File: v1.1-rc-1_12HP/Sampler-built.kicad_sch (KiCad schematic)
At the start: 274 parts, among them J10 Eurorack_Power_10pin_Unshroud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, J11 3.5mm_Mono_Switched, J12 3.5mm_Mono_Switched, J13 3.5mm_Mono_Switched, J14 3.5mm_Mono_Switched, J15 3.5mm_Mono_Switched, J16 3.5mm_Mono_Switched, J17 3.5mm_Mono_Switched, J2 3.5mm_Mono_Switched, J3 Conn_01x04, J4 Conn_02x04, J6 3.5mm_Mono_Switched, J7 3.5mm_Mono_Switched, J8 3.5mm_Mono_Switched, J9 3.5mm_Mono_Switched, U1 TL072H, U10 TL072H, U11 TL072H, U12 TL072H, U13 AP62200WU-7, U15 NJM2068, U16 NJM2068, U17 AZ1117CR-3.3TRG1, U18 STS SD card w/adaptor, U2 STM32F746IE, U3 TL072H, U4 SDRAM_IS42S16400J-6BLI-TR, U5 TL072H, U6 NCP51460SN33, U7 TL072H, U8 TL072H, U9 PCM3060PW, Y1 16MHz_18pF_FA238

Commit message: Proofed and fixed v1.1rc1_12HP schematic. Some schematic TODO left
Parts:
- removed C16, C20, C83, C84: 10nF_0402_16V, 4ms_Capacitor:C_0402, symbol 4ms_Capacitor:10nF_0402_16V
- removed C43: 1uF_0603_25V, 4ms_Capacitor:C_0603, symbol 4ms_Capacitor:1uF_0603_25V
- removed C50: 2.2uF_0603_25V, 4ms_Capacitor:C_0603, symbol 4ms_Capacitor:2.2uF_0603_25V
- removed C65, C66: 100nF_0402_50V, 4ms_Capacitor:C_0402, symbol 4ms_Capacitor:100nF_0402_50V
- removed D10, D11, D12, D13, D14, D2, D27, D28, D30, D4, D5, D6, D8, D9: BAT54S, 4ms_Package_SOT:SOT23-3_PO132, symbol 4ms_Diode:BAT54S
- removed R37: 68Ω_0402, 4ms_Resistor:R_0402, symbol 4ms_Resistor_0402:68Ω_0402
- removed R38: 10k_0603, 4ms_Resistor:R_0603, symbol 4ms_Resistor_0603:10k_0603
- removed R39, R9: 2k_0402, 4ms_Resistor:R_0402, symbol 4ms_Resistor_0402:2k_0402
- removed R69, R72: 1k_0603, 4ms_Resistor:R_0603, symbol 4ms_Resistor_0603:1k_0603
- removed R76: 47k_0603, 4ms_Resistor:R_0603, symbol 4ms_Resistor_0603:47k_0603
- removed S1, S2: SW_Push_PTS526 SM15 SMTR2 LFS, 4ms_Switch:Button_Tact_PTS526, symbol 4ms_Switch:SW_Push_PTS526 SM15 SMTR2 LFS
- removed U17: AZ1117CR-3.3TRG1, 4ms_Package_SOT:SOT89-3, symbol 4ms_Regulator:AZ1117CR-3.3TRG1
- removed unit 2 of U7
- added C? (x2): 100nF_0402_50V, 4ms_Capacitor:C_0402, symbol 4ms_Capacitor:100nF_0402_50V
- C39: value 10nF_0402_16V -> 0.1uF_0603_16V; footprint 4ms_Capacitor:C_0402 -> 4ms_Capacitor:C_0603; symbol 4ms_Capacitor:10nF_0402_16V -> 4ms_Capacitor:0.1uF_0603_16V; Display 10nF -> 0.1uF; JLCPCB ID C15195 -> C14663; Manufacturer Yageo -> AVX Corporation; Part Number CC0402KRX7R7BB103 -> 0603YC104KAT2A; Specifications 10nF, Min. 16V 10%, X7R or X5R or similar -> 0.1uF, Min. 16V 10%, X7R or X5R or similar
- R29: value 10k_0603 -> 20k_0603; symbol 4ms_Resistor_0603:10k_0603 -> 4ms_Resistor_0603:20k_0603; Display 10k -> 20k; JLCPCB ID C98220 -> C105575; Part Number RC0603FR-0710KL -> RC0603FR-0720KL; Specifications 10k, 1%, 1/10W, 0603 -> 20k, 1%, 1/10W, 0603
- R64, R68: value 1k_0603 -> 2k_0402; footprint 4ms_Resistor:R_0603 -> 4ms_Resistor:R_0402; symbol 4ms_Resistor_0603:1k_0603 -> 4ms_Resistor_0402:2k_0402; Display 1k -> 2k; JLCPCB ID C22548 -> C60488; Part Number RC0603FR-071KL -> RC0402FR-072KL; Specifications 1k, 1%, 1/10W, 0603 -> 2k, 1%, 1/16W, 0402
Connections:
- net +12V: now also C?.1
- net -12VA: now also C?.1
- net A0: now also R2.2; no longer R1.1
- net A1: now also R12.2; no longer R11.1
- net A2: now also R19.2; no longer R18.1
- net A6: now also C39.1
- net D12: now also C54.1, R74.2
- net D2: now also C19.1, D7.3 (AK), R58.2
- net DEBUG2: now also J4.5 (Pin_5)
- net DEBUG3: now also J4.7 (Pin_7)
- net GND: now also J13.3 (SW), J14.3 (SW), J4.2 (Pin_2), J4.4 (Pin_4), J4.6 (Pin_6), J4.8 (Pin_8), C?.2, C?.2
- net UART_RX: now also J4.3 (Pin_3)
- net UART_TX: now also J4.1 (Pin_1)
- net BOOT0: now reaches R8.2, U2.D6 (BOOT)
- net NRST: now reaches C15.2, U2.J1 (NRST)
- net at C82.1, D1.3 (AK), R1.2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: no longer R15.2, R2.2, R21.2
- net at R29.2: now also C3.2, R57.1, U15.5 (+)
- net at Bank_But1.8 (B): now also R64.2
- net at R68.2: now also REV_BUT1.7 (R)
- net at REV_BUT1.2 (POLE-A): now also R36.2
- net at C6.1, R56.1, U15.7: now also R18.1; no longer R19.2
- net +5VA renamed +5V
- net USB_DM: no longer names the net of U2.C15 (PA11)
- net USB_DP: no longer names the net of U2.B15 (PA12)
- net USB_ID: no longer names the net of U2.D15 (PA10)
- net USB_VBUS: no longer names the net of U2.E15 (PA9)
- new net: C1.1, POT_PITCH1.2 (Center), R11.1
- new net: R1.1, R15.2, R21.2
- new net: R11.2, U1.5 (+)
- no-connect marks 64 -> 66
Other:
- note added: "4ms Sampler (Built)"
- note added: "Note: do not use the second half of this opamp (U16) for anything."
- note added: "TODO: Consolidate CV op-amps based on where they are placed on PCB. Use a single opamp if needed (most likely for PitchCV)"
- note added: "TODO: Use single op-amps for pots"
- note added: "TODO: make all of these like Pitch Pot"
- note added: "TODO: make all of these like StartCV"
- note removed: "4ms Sampler Kit"
- note removed: "I2C4_SCL"
- note removed: "I2C4_SDA"
- note removed: "SPI2_MISO"
- note removed: "SPI2_MOSI"
- note removed: "SPI2_NSS"
- note removed: "SPI2_SCK"
- moved on the sheet: C1, C12, C13, C14, C15, C17, C18, C19, C21, C22, C23, C24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

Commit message: v1.1-rc1-12HP: part placement and routing ip
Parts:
- removed C47, C87, C88: 10nF_0402_16V, 4ms_Capacitor:C_0402, symbol 4ms_Capacitor:10nF_0402_16V
- removed C? (x2): 100nF_0402_50V, 4ms_Capacitor:C_0402, symbol 4ms_Capacitor:100nF_0402_50V
- removed D18, D31, D32: BAT54S, 4ms_Package_SOT:SOT23-3_PO132, symbol 4ms_Diode:BAT54S
- removed unit 3 of U7
- added C87, C88: 100nF_0402_50V, 4ms_Capacitor:C_0402, symbol 4ms_Capacitor:100nF_0402_50V
- added unit 1 of U14
- added unit 3 of U14
- C35: renamed from C13; value 0.1uF_0603_16V -> 100nF_0402_50V; footprint 4ms_Capacitor:C_0603 -> 4ms_Capacitor:C_0402; symbol 4ms_Capacitor:0.1uF_0603_16V -> 4ms_Capacitor:100nF_0402_50V; Alt JLCPCB ID (none) -> C77020; JLCPCB ID C14663 -> C307331; Manufacturer AVX Corporation -> Murata; Part Number 0603YC104KAT2A -> GRM155R71H104KE14D; Specifications 0.1uF, Min. 16V 10%, X7R or X5R or similar -> 0.1uF, Min. 50V 10%, X7R or X5R or similar
- C37: renamed from C14; value 0.1uF_0603_16V -> 100nF_0402_50V; footprint 4ms_Capacitor:C_0603 -> 4ms_Capacitor:C_0402; symbol 4ms_Capacitor:0.1uF_0603_16V -> 4ms_Capacitor:100nF_0402_50V; Alt JLCPCB ID (none) -> C77020; JLCPCB ID C14663 -> C307331; Manufacturer AVX Corporation -> Murata; Part Number 0603YC104KAT2A -> GRM155R71H104KE14D; Specifications 0.1uF, Min. 16V 10%, X7R or X5R or similar -> 0.1uF, Min. 50V 10%, X7R or X5R or similar
- C38: renamed from C17; value 0.1uF_0603_16V -> 100nF_0402_50V; footprint 4ms_Capacitor:C_0603 -> 4ms_Capacitor:C_0402; symbol 4ms_Capacitor:0.1uF_0603_16V -> 4ms_Capacitor:100nF_0402_50V; Alt JLCPCB ID (none) -> C77020; JLCPCB ID C14663 -> C307331; Manufacturer AVX Corporation -> Murata; Part Number 0603YC104KAT2A -> GRM155R71H104KE14D; Specifications 0.1uF, Min. 16V 10%, X7R or X5R or similar -> 0.1uF, Min. 50V 10%, X7R or X5R or similar
- C40: renamed from C18; value 0.1uF_0603_16V -> 100nF_0402_50V; footprint 4ms_Capacitor:C_0603 -> 4ms_Capacitor:C_0402; symbol 4ms_Capacitor:0.1uF_0603_16V -> 4ms_Capacitor:100nF_0402_50V; Alt JLCPCB ID (none) -> C77020; JLCPCB ID C14663 -> C307331; Manufacturer AVX Corporation -> Murata; Part Number 0603YC104KAT2A -> GRM155R71H104KE14D; Specifications 0.1uF, Min. 16V 10%, X7R or X5R or similar -> 0.1uF, Min. 50V 10%, X7R or X5R or similar
- R13, R3, R35, R5, R64, R68: value 2k_0402 -> 2k_0603; footprint 4ms_Resistor:R_0402 -> 4ms_Resistor:R_0603; symbol 4ms_Resistor_0402:2k_0402 -> 4ms_Resistor_0603:2k_0603; JLCPCB ID C60488 -> C105576; Part Number RC0402FR-072KL -> RC0603FR-072KL; Specifications 2k, 1%, 1/16W, 0402 -> 2k, 1%, 1/10W, 0603
- R36: value 10k_0402 -> 10k_0603; footprint 4ms_Resistor:R_0402 -> 4ms_Resistor:R_0603; symbol 4ms_Resistor_0402:10k_0402 -> 4ms_Resistor_0603:10k_0603; JLCPCB ID C60490 -> C98220; Part Number RC0402FR-0710KL -> RC0603FR-0710KL; Specifications 10k, 1%, 1/16W, 0402 -> 10k, 1%, 1/10W, 0603
- renumbered C21 to C1, C31 to C10, C33 to C11, C35 to C12, C36 to C13, C37 to C14, C38 to C17, C79 to C18, C23 to C2, C4 to C21, C89 to C23, C5 to C24, C10 to C25, C11 to C26, C91 to C27, C92 to C28, C24 to C3, C93 to C30, C95 to C31, C96 to C33, C42 to C36, C25 to C4, C3 to C42, C46 to C43, C6 to C46, C53 to C47, C26 to C5, C94 to C50, C40 to C53, C27 to C6, C7 to C65, C9 to C66, C28 to C7, C2 to C79, C1 to C83, C12 to C84, C30 to C9, R31 to R4, R4 to R9, U10 to U1, U1 to U10, U5 to U10, U3 to U14, U10 to U3, U7 to U5
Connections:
- net +12V: now also C87.1, U14.8 (V+)
- net -12VA: now also C88.1, U14.4 (V-)
- net A3: now also R23.2; no longer R22.1
- net A4: now also R28.2; no longer R27.1
- net A5: now also R81.2; no longer R30.1
- net A7: now also R41.2; no longer R40.1
- net A8: now also R34.2; no longer R33.1
- net A9: now also R46.2; no longer R45.1
- net GND: now also U16.3 (+), C87.2, C88.2, U14.2 (-); no longer U16.5 (+)
- net at R20.2, R26.2: now also R27.1; no longer R28.2
- net at C84.2, R62.2, R63.1: now also U16.7; no longer U16.1
- net at R16.2, R24.2: now also R30.1; no longer R81.2
- net at C84.1, R61.2, R62.1: now also U16.6 (-); no longer U16.2 (-)
- net at R17.2, R25.2: now also R33.1; no longer R34.2
- net at R45.2: now also U3.3 (+); no longer U3.5 (+)
- net at R60.2: now also U16.5 (+); no longer U16.3 (+)
- net at R17.1: now also J9.1 (SIG); no longer J7.1 (SIG)
- net at C79.1, POT_SAMP1.2 (Center): now also R45.1; no longer R46.2
- net at C97.1, D15.3 (AK), R18.2: now also U14.5 (+); no longer U14.3 (+)
- net at C85.1, D26.3 (AK), R33.2: now also U5.5 (+); no longer U5.3 (+)
- net at R20.1: now also J7.1 (SIG); no longer J9.1 (SIG)
- new net: C66.1, POT_LENGTH1.2 (Center), R22.1
- new net: R46.1, U3.1, U3.2 (-)
- new net: U14.1, U14.3 (+)
- new net: C65.1, POT_START1.2 (Center), R40.1
- new net: R34.1, U5.6 (-), U5.7
- new net: R19.1, U14.6 (-), U14.7
- new net: U16.1, U16.2 (-)
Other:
- note removed: "Length_Pot"
- note removed: "Pitch_Pot"
- note removed: "Sample_Pot"
- note removed: "Start_Pot"
- note removed: "TODO: make all of these like Pitch Pot"
- note removed: "TODO: make all of these like StartCV"
- moved on the sheet: C42, C46, C65, C66, C79, C97, D15, J6, J7, J8, J9, POT_LENGTH1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

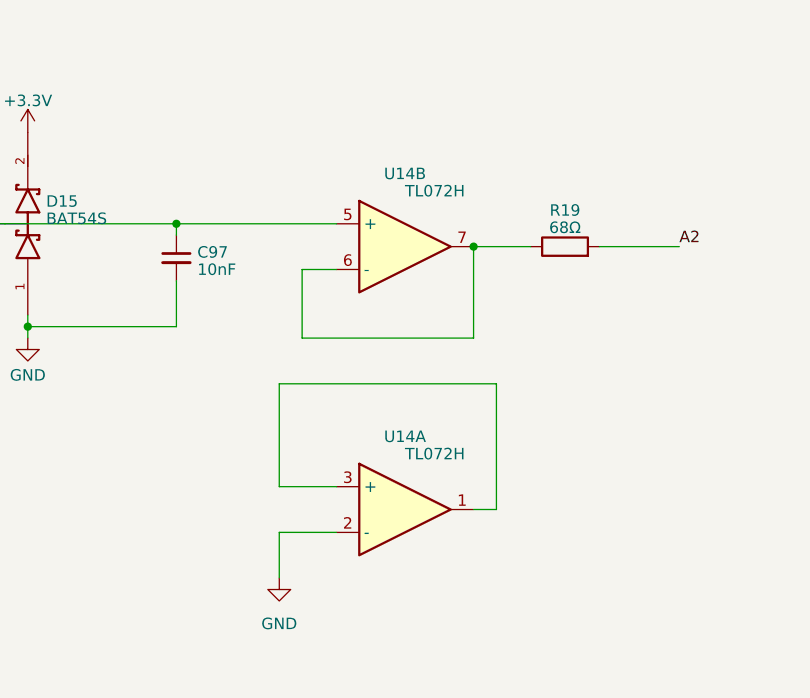
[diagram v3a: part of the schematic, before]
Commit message: Updates to pcb / routing for noise mitigation
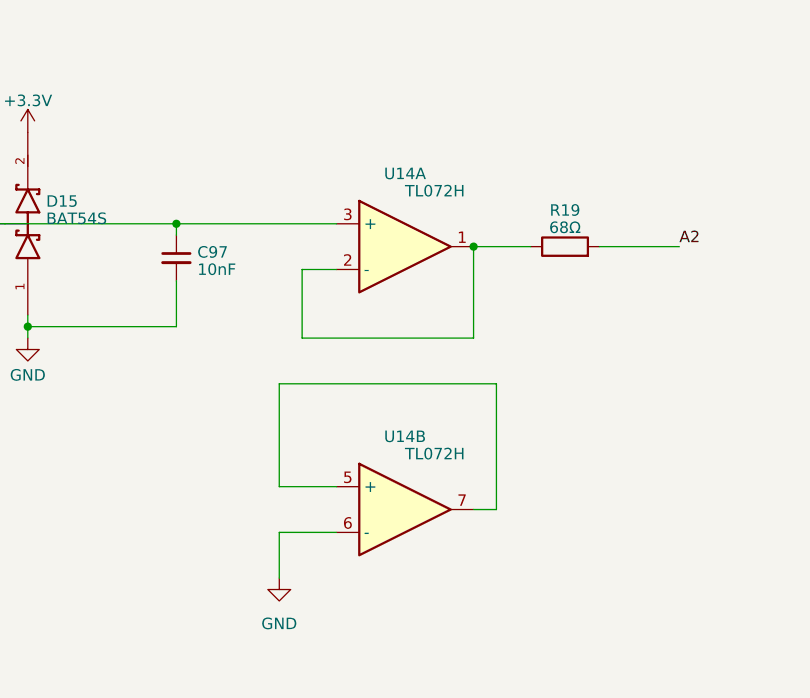
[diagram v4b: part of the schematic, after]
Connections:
- net GND: now also U14.6 (-); no longer U14.2 (-)
- net at C97.1, D15.3 (AK), R18.2: now also U14.3 (+); no longer U14.5 (+)
- new net: U14.5 (+), U14.7
- new net: R19.1, U14.1, U14.2 (-)
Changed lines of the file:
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@@
     )
   )
-  (symbol (lib_id "4ms_IC:TL072H") (at 831.85 632.46 0) (unit 1)
+  (symbol (lib_id "4ms_IC:TL072H") (at 831.85 632.46 0) (unit 2)
     (in_bom yes) (on_board yes) (dnp no) (fields_autoplaced)
     (property "Reference" "U14" (at 831.85 624.3701 0)
@@
       (project "Sampler-built"
         (path "/39a72d2b-4494-42c9-aa7a-6ac21ca5673f"
-          (reference "U14") (unit 1)
+          (reference "U14") (unit 2)
         )
       )
@@
     )
   )
-  (symbol (lib_id "4ms_IC:TL072H") (at 831.85 603.25 0) (unit 2)
+  (symbol (lib_id "4ms_IC:TL072H") (at 831.85 603.25 0) (unit 1)
     (in_bom yes) (on_board yes) (dnp no) (fields_autoplaced)
     (property "Reference" "U14" (at 831.85 595.1601 0)
@@
       (project "Sampler-built"
         (path "/39a72d2b-4494-42c9-aa7a-6ac21ca5673f"
-          (reference "U14") (unit 2)
+          (reference "U14") (unit 1)
         )
       )
